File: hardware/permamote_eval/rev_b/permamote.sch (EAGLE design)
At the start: 136 parts, among them J1 TC2030-JLINK-L, J2 M10X2, J3 M04X2, Q1 PMDXB950UPEL, Q10 CSD22206W, Q11 CSD22206W, Q2 PMDXB950UPEL, Q3 PMDXB950UPEL, Q4 PMDXB950UPEL, Q5 PMDXB950UPEL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

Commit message: WIP reroute signals
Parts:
- removed Q11, Q9: CSD22206W, fets:CSD22206W
- added C41: 0.1uF, passives:CAPACITOR0402_CAP
- added J5: MICRO_USB_B_HIROSE_ZX62R-B-5P, connector:MICRO_USB_B_HIROSE_ZX62R-B-5P
- added U12: FT232RQ, ftdichip:FT232RQ
- BT2, BT3: value BAT-HLD-20XX-THRU -> BAT-HLD-002-THM; device batteries:BAT-HLD-20XX-THRU -> batteries:BAT-HLD-002-THM
- C17: device passives:CAPACITOR0603_CAP -> passives:CAPACITOR0402_CAP
- D1: value SOLARCELL -> SOLARCELLSCREW; device mote:SOLARCELL -> permamote:SOLARCELLSCREW
- Q10, Q7, Q8: value CSD22206W -> PMDXB950UPEL; device fets:CSD22206W -> fets:PMDXB950UPEL
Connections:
- net N$46 renamed !VBAT_SEC_ON
- net N$56 renamed !VBAT_PRI_ON
- removed net !ACC_EN: J2.15, U10.P1.15, U9.P16
- removed net !I2C_EN: J2.3
- new net D+: J5.D+, U12.USBDP
- new net D-: J5.D-, U12.USBDM
- new net DBG_RX: J2.5, U10.P1.09, U12.TXD, U9.P24
- new net DBG_TX: J2.7, U10.P0.12, U12.RXD, U9.P25
- new net N$13: C41.1, U12.3V3OUT
- new net USB_5V: J5.+5V, U12.VCC
- net !CLR_EN: now also J2.11, Q7.1.G; no longer J2.9, Q7.G
- net !HUM_EN: now also Q8.2.G, U10.P0.10/NFC2; no longer Q10.G, U10.P0.12
- net !LT_EN: now also J2.13, Q7.2.G; no longer J2.11, Q8.G
- net !PIR_EN: now also J2.15, Q10.1.G; no longer J2.13, Q11.G
- net !PR_EN: now also J2.9, Q8.1.G; no longer J2.7, Q9.G
- net !RST: now also U12.!RESET
- net !RTC_IRQ1: no longer U9.P25
- net !RTC_IRQ2: no longer U9.P24
- net GND: now also C41.2, J5.GND, U12.GND, U12.GND@1, U12.GND@2, U12.GND@A, U12.TEST
- net MOSI: now also J2.3; no longer J2.5
- net N$19: now also Q8.1.S; no longer Q9.S
- net N$20: now also Q7.2.D; no longer Q8.D
- net N$21: now also Q8.1.D; no longer Q9.D
- net N$22: now also Q8.2.D; no longer Q10.D
- net N$23: now also Q10.1.D; no longer Q11.D
- net N$24: now also Q10.1.S; no longer Q11.S
- net N$31: now also Q7.1.D; no longer Q7.D
- net N$33: now also Q7.1.S; no longer Q7.S
- net N$36: now also Q8.2.S; no longer Q10.S
- net N$37: now also Q7.2.S; no longer Q8.S
- net VCC: now also U12.VCCIO
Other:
- moved on the sheet: BT2, BT3, H1, H2, H3, H4, J2, J3, J4

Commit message: WIP route test signals + change rtc source
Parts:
- added JP17, JP18: (no value), SparkFun-Passives:JUMPER-2SMD-NC
- added JP19: (no value), SparkFun-Connectors:M02PTH
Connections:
- new net N$46: JP17.1, U12.!RESET
- new net N$56: JP18.1, JP19.1, U1.VBAT
- net !RST: now also JP17.2; no longer U12.!RESET
- net VBAT: now also JP18.2, JP19.2; no longer JP10.2, JP6.2, R6.2, R7.2
- net VCC: now also JP10.2, JP6.2, R6.2, R7.2
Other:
- moved on the sheet: J1, JP10, JP6

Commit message: Rearrange some labels, notes
Note that i2c pullups do not need to be populated
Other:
- note added: "Do not populate. Nordic chips have internal pullup."
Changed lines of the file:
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@@
 <grid distance="0.1" unitdist="inch" unit="inch" style="lines" multiple="1" display="no" altdistance="0.01" altunitdist="inch" altunit="inch"/>
 <layers>
-<layer number="1" name="Top" color="4" fill="1" visible="yes" active="no"/>
-<layer number="2" name="Route2" color="14" fill="1" visible="yes" active="no"/>
-<layer number="3" name="Route3" color="4" fill="3" visible="yes" active="no"/>
-<layer number="4" name="Route4" color="1" fill="4" visible="yes" active="no"/>
-<layer number="5" name="Route5" color="4" fill="4" visible="yes" active="no"/>
-<layer number="6" name="Route6" color="1" fill="8" visible="yes" active="no"/>
-<layer number="7" name="Route7" color="4" fill="8" visible="yes" active="no"/>
-<layer number="8" name="Route8" color="1" fill="2" visible="yes" active="no"/>
-<layer number="9" name="Route9" color="4" fill="2" visible="yes" active="no"/>
-<layer number="10" name="Route10" color="1" fill="7" visible="yes" active="no"/>
-<layer number="11" name="Route11" color="4" fill="7" visible="yes" active="no"/>
-<layer number="12" name="Route12" color="1" fill="5" visible="yes" active="no"/>
-<layer number="13" name="Route13" color="4" fill="5" visible="yes" active="no"/>
-<layer number="14" name="Route14" color="1" fill="6" visible="yes" active="no"/>
-<layer number="15" name="Route15" color="11" fill="1" visible="yes" active="no"/>
-<layer number="16" name="Bottom" color="1" fill="1" visible="yes" active="no"/>
-<layer number="17" name="Pads" color="2" fill="1" visible="yes" active="no"/>
-<layer number="18" name="Vias" color="2" fill="1" visible="yes" active="no"/>
-<layer number="19" name="Unrouted" color="6" fill="1" visible="yes" active="no"/>
-<layer number="20" name="Dimension" color="24" fill="1" visible="yes" active="no"/>
-<layer number="21" name="tPlace" color="7" fill="1" visible="yes" active="no"/>
-<layer number="22" name="bPlace" color="7" fill="1" visible="yes" active="no"/>
-<layer number="23" name="tOrigins" color="15" fill="1" visible="yes" active="no"/>
-<layer number="24" name="bOrigins" color="15" fill="1" visible="yes" active="no"/>
-<layer number="25" name="tNames" color="7" fill="1" visible="yes" active="no"/>
-<layer number="26" name="bNames" color="7" fill="1" visible="yes" active="no"/>
-<layer number="27" name="tValues" color="7" fill="1" visible="yes" active="no"/>
-<layer number="28" name="bValues" color="7" fill="1" visible="yes" active="no"/>
+<layer number="1" name="Top" color="4" fill="1" visible="no" active="no"/>
+<layer number="2" name="Route2" color="14" fill="1" visible="no" active="no"/>
+<layer number="3" name="Route3" color="4" fill="3" visible="no" active="no"/>
+<layer number="4" name="Route4" color="1" fill="4" visible="no" active="no"/>
+<layer number="5" name="Route5" color="4" fill="4" visible="no" active="no"/>
+<layer number="6" name="Route6" color="1" fill="8" visible="no" active="no"/>
+<layer number="7" name="Route7" color="4" fill="8" visible="no" active="no"/>
+<layer number="8" name="Route8" color="1" fill="2" visible="no" active="no"/>
+<layer number="9" name="Route9" color="4" fill="2" visible="no" active="no"/>
+<layer number="10" name="Route10" color="1" fill="7" visible="no" active="no"/>
+<layer number="11" name="Route11" color="4" fill="7" visible="no" active="no"/>
+<layer number="12" name="Route12" color="1" fill="5" visible="no" active="no"/>
+<layer number="13" name="Route13" color="4" fill="5" visible="no" active="no"/>
+<layer number="14" name="Route14" color="1" fill="6" visible="no" active="no"/>
+<layer number="15" name="Route15" color="11" fill="1" visible="no" active="no"/>
+<layer number="16" name="Bottom" color="1" fill="1" visible="no" active="no"/>
+<layer number="17" name="Pads" color="2" fill="1" visible="no" active="no"/>
+<layer number="18" name="Vias" color="2" fill="1" visible="no" active="no"/>
+<layer number="19" name="Unrouted" color="6" fill="1" visible="no" active="no"/>
+<layer number="20" name="Dimension" color="24" fill="1" visible="no" active="no"/>
+<layer number="21" name="tPlace" color="7" fill="1" visible="no" active="no"/>
+<layer number="22" name="bPlace" color="7" fill="1" visible="no" active="no"/>
+<layer number="23" name="tOrigins" color="15" fill="1" visible="no" active="no"/>
+<layer number="24" name="bOrigins" color="15" fill="1" visible="no" active="no"/>
+<layer number="25" name="tNames" color="7" fill="1" visible="no" active="no"/>
+<layer number="26" name="bNames" color="7" fill="1" visible="no" active="no"/>
+<layer number="27" name="tValues" color="7" fill="1" visible="no" active="no"/>
+<layer number="28" name="bValues" color="7" fill="1" visible="no" active="no"/>
 <layer number="29" name="tStop" color="7" fill="3" visible="no" active="no"/>
 <layer number="30" name="bStop" color="7" fill="6" visible="no" active="no"/>
@@
 <layer number="35" name="tGlue" color="7" fill="4" visible="no" active="no"/>
 <layer number="36" name="bGlue" color="7" fill="5" visible="no" active="no"/>
-<layer number="37" name="tTest" color="7" fill="1" visible="yes" active="no"/>
-<layer number="38" name="bTest" color="7" fill="1" visible="yes" active="no"/>
+<layer number="37" name="tTest" color="7" fill="1" visible="no" active="no"/>
+<layer number="38" name="bTest" color="7" fill="1" visible="no" active="no"/>
 <layer number="39" name="tKeepout" color="4" fill="11" visible="no" active="no"/>
 <layer number="40" name="bKeepout" color="1" fill="11" visible="no" active="no"/>
@@
 <layer number="44" name="Drills" color="7" fill="1" visible="no" active="no"/>
 <layer number="45" name="Holes" color="7" fill="1" visible="no" active="no"/>
-<layer number="46" name="Milling" color="3" fill="1" visible="yes" active="no"/>
-<layer number="47" name="Measures" color="7" fill="1" visible="yes" active="no"/>
-<layer number="48" name="Document" color="7" fill="1" visible="yes" active="no"/>
-<layer number="49" name="Reference" color="7" fill="1" visible="yes" active="no"/>
-<layer number="50" name="dxf" color="7" fill="1" visible="yes" active="no"/>
-<layer number="51" name="tDocu" color="7" fill="1" visible="yes" active="no"/>
-<layer number="52" name="bDocu" color="7" fill="1" visible="yes" active="no"/>
-<layer number="53" name="tGND_GNDA" color="7" fill="9" visible="yes" active="no"/>
-<layer number="54" name="bGND_GNDA" color="1" fill="9" visible="yes" active="no"/>
-<layer number="56" name="wert" color="7" fill="1" visible="yes" active="no"/>
-<layer number="57" name="tCAD" color="7" fill="1" visible="yes" active="no"/>
-<layer number="59" name="Invisible" color="7" fill="1" visible="yes" active="no"/>
-<layer number="60" name="bCarbon" color="7" fill="1" visible="yes" active="no"/>
-<layer number="61" name="stand" color="7" fill="1" visible="yes" active="no"/>
+<layer number="46" name="Milling" color="3" fill="1" visible="no" active="no"/>
+<layer number="47" name="Measures" color="7" fill="1" visible="no" active="no"/>
+<layer number="48" name="Document" color="7" fill="1" visible="no" active="no"/>
+<layer number="49" name="Reference" color="7" fill="1" visible="no" active="no"/>
+<layer number="50" name="dxf" color="7" fill="1" visible="no" active="no"/>
+<layer number="51" name="tDocu" color="7" fill="1" visible="no" active="no"/>
+<layer number="52" name="bDocu" color="7" fill="1" visible="no" active="no"/>
+<layer number="53" name="tGND_GNDA" color="7" fill="9" visible="no" active="no"/>
+<layer number="54" name="bGND_GNDA" color="1" fill="9" visible="no" active="no"/>
+<layer number="56" name="wert" color="7" fill="1" visible="no" active="no"/>
+<layer number="57" name="tCAD" color="7" fill="1" visible="no" active="no"/>
+<layer number="59" name="Invisible" color="7" fill="1" visible="no" active="no"/>
+<layer number="60" name="bCarbon" color="7" fill="1" visible="no" active="no"/>
+<layer number="61" name="stand" color="7" fill="1" visible="no" active="no"/>
 <layer number="90" name="Modules" color="5" fill="1" visible="yes" active="yes"/>
 <layer number="91" name="Nets" color="2" fill="1" visible="yes" active="yes"/>
@@
 Either populate the NRF52840
 (Page 1) or NRF51822 (Page 2)</text>
+<text x="223.52" y="119.38" size="1.778" layer="98">Do not populate.
+Nordic chips have
+internal pullup.</text>
 </plain>
 <instances>

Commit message: incorporate Branden's changes
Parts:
- added JP20, JP21, JP22: (no value), SparkFun-Passives:JUMPER-2SMD-NC
- JP17: device SparkFun-Passives:JUMPER-2SMD-NC -> SparkFun-Passives:JUMPER-2SMD-NO
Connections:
- net N$13 renamed 3V3OUT
- removed net N$20: Q7.2.D, U7.VCC
- new net N$13: JP22.2, U12.VCCIO
- new net N$59: Q7.2.D, R5.2, U7.VCC
- new net RXD: JP21.1, U12.RXD
- new net TXD: JP20.1, U12.TXD
- net DBG_RX: now also JP20.2; no longer U12.TXD
- net DBG_TX: now also JP21.2; no longer U12.RXD
- net N$31: now also R4.2
- net N$33: no longer R4.2
- net N$37: no longer R5.2
- net VCC: now also JP22.1; no longer U12.VCCIO
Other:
- moved on the sheet: C32, R4, R5

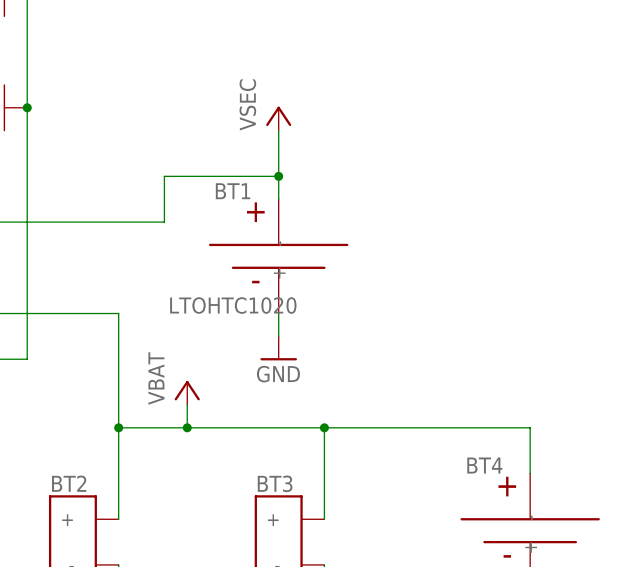
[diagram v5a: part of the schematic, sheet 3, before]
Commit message: add vanadium battery
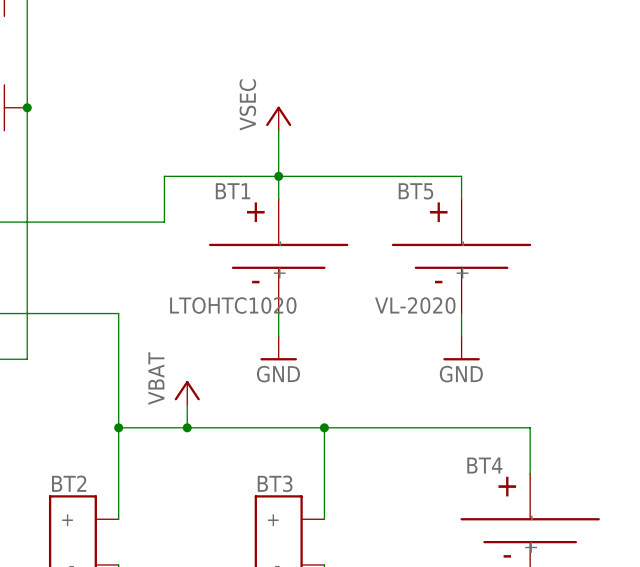
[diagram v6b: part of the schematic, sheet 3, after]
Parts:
- added BT5: VL-2020, batteries:VL-2020
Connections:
- net GND: now also BT5.-
- net VSEC: now also BT5.+
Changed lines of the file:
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@@
 <part name="JP21" library="SparkFun-Passives" deviceset="JUMPER-2" device="SMD-NC"/>
 <part name="JP22" library="SparkFun-Passives" deviceset="JUMPER-2" device="SMD-NC"/>
+<part name="BT5" library="batteries" deviceset="VL" device="-2020"/>
+<part name="GND34" library="supply1" library_urn="urn:adsk.eagle:library:371" deviceset="GND" device=""/>
 </parts>
 <sheets>
@@
 <instance part="L8" gate="G$1" x="48.26" y="63.5" rot="R90"/>
 <instance part="D1" gate="G$1" x="50.8" y="137.16"/>
+<instance part="BT5" gate="G$1" x="236.22" y="144.78"/>
+<instance part="GND34" gate="1" x="236.22" y="134.62"/>
 </instances>
 <busses>
@@
 <pinref part="R16" gate="G$1" pin="1"/>
 <wire x1="172.72" y1="30.48" x2="172.72" y2="40.64" width="0.1524" layer="91"/>
+</segment>
+<segment>
+<pinref part="BT5" gate="G$1" pin="-"/>
+<wire x1="236.22" y1="139.7" x2="236.22" y2="137.16" width="0.1524" layer="91"/>
+<pinref part="GND34" gate="1" pin="GND"/>
 </segment>
 </net>
@@
 <wire x1="152.4" y1="149.86" x2="203.2" y2="149.86" width="0.1524" layer="91"/>
 <wire x1="203.2" y1="149.86" x2="203.2" y2="154.94" width="0.1524" layer="91"/>
-</segment>
-</net>
+<pinref part="BT5" gate="G$1" pin="+"/>
+<wire x1="215.9" y1="154.94" x2="236.22" y2="154.94" width="0.1524" layer="91"/>
+<wire x1="236.22" y1="154.94" x2="236.22" y2="152.4" width="0.1524" layer="91"/>
+</segment>
+</net>
